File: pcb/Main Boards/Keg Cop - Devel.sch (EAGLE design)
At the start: 24 parts

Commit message: Add proper value for R6
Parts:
- R6: value 2.2kΩ -> 200kΩ
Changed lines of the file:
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@@
 <part name="SOLENOID" library="adafruit" library_urn="urn:adsk.eagle:library:420" deviceset="LED" device="3MM" package3d_urn="urn:adsk.eagle:package:6240537/1"/>
 <part name="COOL" library="adafruit" library_urn="urn:adsk.eagle:library:420" deviceset="LED" device="3MM" package3d_urn="urn:adsk.eagle:package:6240537/1"/>
-<part name="R6" library="SparkFun-Resistors" library_urn="urn:adsk.eagle:library:532" deviceset="RESISTOR" device="AXIAL-0.3" package3d_urn="urn:adsk.eagle:package:39658/1" value="2.2kΩ"/>
+<part name="R6" library="SparkFun-Resistors" library_urn="urn:adsk.eagle:library:532" deviceset="RESISTOR" device="AXIAL-0.3" package3d_urn="urn:adsk.eagle:package:39658/1" value="200kΩ"/>
 <part name="KEG" library="SparkFun-Sensors" deviceset="DS18B20" device=""/>
 <part name="LOWER" library="SparkFun-Sensors" deviceset="DS18B20" device=""/>

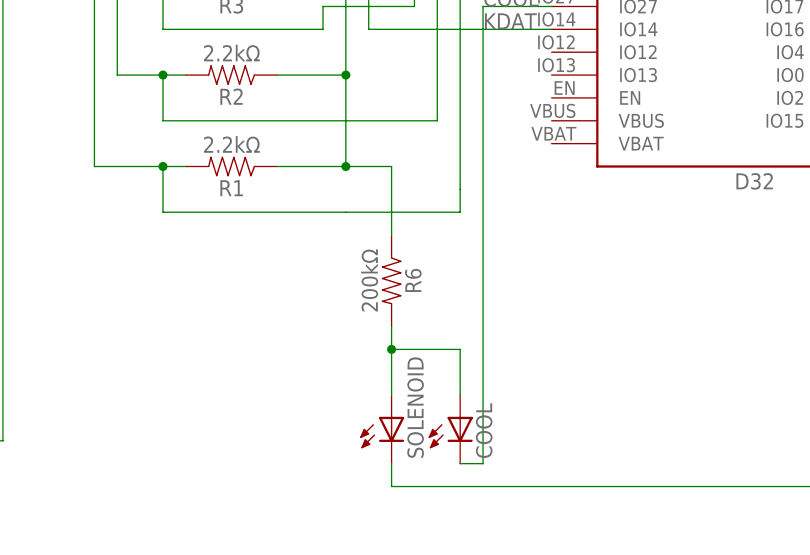
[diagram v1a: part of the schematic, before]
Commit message: Add separate power for sol/cool
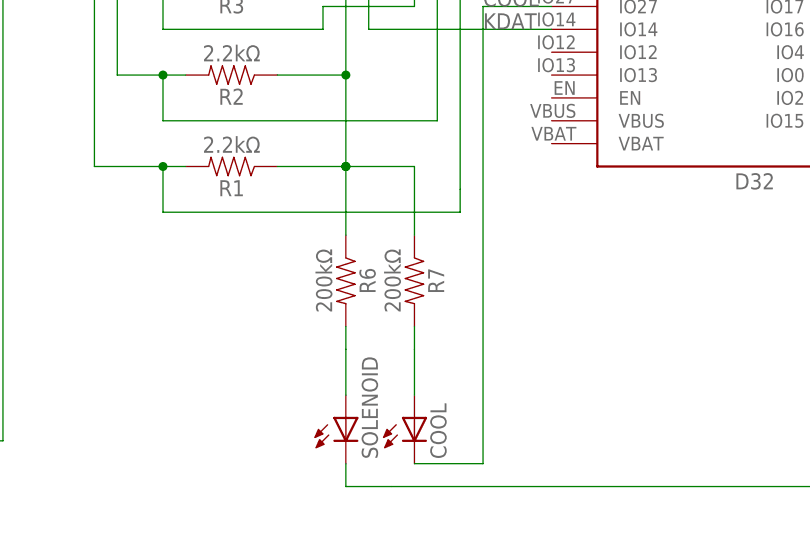
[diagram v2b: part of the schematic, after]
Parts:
- added R7: 200kΩ, SparkFun-Resistors:RESISTORAXIAL-0.3
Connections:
- new net N$1: COOL.A, R7.2
- net 3V3: now also R7.1
- net N$2: no longer COOL.A
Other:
- moved on the sheet: COOL, R6, SOLENOID
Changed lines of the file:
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@@
 <?xml version="1.0" encoding="utf-8"?>
 <!DOCTYPE eagle SYSTEM "eagle.dtd">
-<eagle version="9.5.2">
+<eagle version="9.6.2">
 <drawing>
 <settings>
@@
 <part name="TOWER" library="SparkFun-Sensors" deviceset="DS18B20" device=""/>
 <part name="ROOM" library="SparkFun-Sensors" deviceset="DS18B20" device=""/>
+<part name="R7" library="SparkFun-Resistors" library_urn="urn:adsk.eagle:library:532" deviceset="RESISTOR" device="AXIAL-0.3" package3d_urn="urn:adsk.eagle:package:39658/1" value="200kΩ"/>
 </parts>
 <sheets>
@@
 <attribute name="VALUE" x="76.835" y="100.33" size="1.778" layer="96"/>
 </instance>
-<instance part="SOLENOID" gate="G$1" x="-7.62" y="0" smashed="yes">
-<attribute name="NAME" x="-4.064" y="-4.572" size="1.778" layer="95" rot="R90"/>
-<attribute name="VALUE" x="-1.905" y="-4.572" size="1.778" layer="96" rot="R90"/>
-</instance>
-<instance part="COOL" gate="G$1" x="0" y="0" smashed="yes">
-<attribute name="NAME" x="3.556" y="-4.572" size="1.778" layer="95" rot="R90"/>
-<attribute name="VALUE" x="5.715" y="-4.572" size="1.778" layer="96" rot="R90"/>
-</instance>
-<instance part="R6" gate="G$1" x="-7.62" y="15.24" smashed="yes" rot="R270">
-<attribute name="NAME" x="-6.096" y="15.24" size="1.778" layer="95" font="vector" rot="R270" align="bottom-center"/>
-<attribute name="VALUE" x="-9.144" y="15.24" size="1.778" layer="96" font="vector" rot="R270" align="top-center"/>
+<instance part="SOLENOID" gate="G$1" x="-12.7" y="0" smashed="yes">
+<attribute name="NAME" x="-9.144" y="-4.572" size="1.778" layer="95" rot="R90"/>
+<attribute name="VALUE" x="-6.985" y="-4.572" size="1.778" layer="96" rot="R90"/>
+</instance>
+<instance part="COOL" gate="G$1" x="-5.08" y="0" smashed="yes">
+<attribute name="NAME" x="-1.524" y="-4.572" size="1.778" layer="95" rot="R90"/>
+<attribute name="VALUE" x="0.635" y="-4.572" size="1.778" layer="96" rot="R90"/>
+</instance>
+<instance part="R6" gate="G$1" x="-12.7" y="15.24" smashed="yes" rot="R270">
+<attribute name="NAME" x="-11.176" y="15.24" size="1.778" layer="95" font="vector" rot="R270" align="bottom-center"/>
+<attribute name="VALUE" x="-14.224" y="15.24" size="1.778" layer="96" font="vector" rot="R270" align="top-center"/>
 </instance>
 <instance part="KEG" gate="G$1" x="-73.66" y="78.74" smashed="yes" rot="R180">
@@
 <attribute name="NAME" x="-66.04" y="-10.414" size="1.778" layer="95" font="vector" rot="R180"/>
 <attribute name="VALUE" x="-66.04" y="5.334" size="1.778" layer="96" font="vector" rot="R180" align="top-left"/>
+</instance>
+<instance part="R7" gate="G$1" x="-5.08" y="15.24" smashed="yes" rot="R270">
+<attribute name="NAME" x="-3.556" y="15.24" size="1.778" layer="95" font="vector" rot="R270" align="bottom-center"/>
+<attribute name="VALUE" x="-6.604" y="15.24" size="1.778" layer="96" font="vector" rot="R270" align="top-center"/>
 </instance>
 </instances>
@@
 <label x="-48.26" y="63.5" size="1.778" layer="95"/>
 <pinref part="R6" gate="G$1" pin="1"/>
-<wire x1="-7.62" y1="20.32" x2="-7.62" y2="27.94" width="0.1524" layer="91"/>
-<wire x1="-7.62" y1="27.94" x2="-12.7" y2="27.94" width="0.1524" layer="91"/>
+<wire x1="-12.7" y1="20.32" x2="-12.7" y2="27.94" width="0.1524" layer="91"/>
 <junction x="-12.7" y="27.94"/>
 <pinref part="KEG" gate="G$1" pin="VDD"/>
@@
 <wire x1="-48.26" y1="63.5" x2="-58.42" y2="63.5" width="0.1524" layer="91"/>
 <junction x="-58.42" y="63.5"/>
+<pinref part="R7" gate="G$1" pin="1"/>
+<wire x1="-5.08" y1="20.32" x2="-5.08" y2="27.94" width="0.1524" layer="91"/>
+<wire x1="-5.08" y1="27.94" x2="-12.7" y2="27.94" width="0.1524" layer="91"/>
+<junction x="-12.7" y="27.94"/>
 </segment>
 </net>
@@
 <label x="2.54" y="45.72" size="1.778" layer="95"/>
 <wire x1="2.54" y1="45.72" x2="2.54" y2="-5.08" width="0.1524" layer="91"/>
-<wire x1="0" y1="-5.08" x2="2.54" y2="-5.08" width="0.1524" layer="91"/>
+<wire x1="-5.08" y1="-5.08" x2="2.54" y2="-5.08" width="0.1524" layer="91"/>
 <pinref part="COOL" gate="G$1" pin="C"/>
 </segment>
@@
 <wire x1="-7.62" y1="-7.62" x2="55.88" y2="-7.62" width="0.1524" layer="91"/>
 <pinref part="SOLENOID" gate="G$1" pin="C"/>
-<wire x1="-7.62" y1="-5.08" x2="-7.62" y2="-7.62" width="0.1524" layer="91"/>
+<wire x1="-12.7" y1="-5.08" x2="-12.7" y2="-7.62" width="0.1524" layer="91"/>
+<wire x1="-12.7" y1="-7.62" x2="-7.62" y2="-7.62" width="0.1524" layer="91"/>
 </segment>
 </net>
 <net name="N$2" class="0">
 <segment>
-<wire x1="0" y1="7.62" x2="-7.62" y2="7.62" width="0.1524" layer="91"/>
 <pinref part="R6" gate="G$1" pin="2"/>
-<wire x1="-7.62" y1="7.62" x2="-7.62" y2="10.16" width="0.1524" layer="91"/>
+<wire x1="-12.7" y1="7.62" x2="-12.7" y2="10.16" width="0.1524" layer="91"/>
 <pinref part="SOLENOID" gate="G$1" pin="A"/>
-<wire x1="-7.62" y1="2.54" x2="-7.62" y2="7.62" width="0.1524" layer="91"/>
-<junction x="-7.62" y="7.62"/>
+<wire x1="-12.7" y1="2.54" x2="-12.7" y2="7.62" width="0.1524" layer="91"/>
+</segment>
+</net>
+<net name="N$1" class="0">
+<segment>
 <pinref part="COOL" gate="G$1" pin="A"/>
-<wire x1="0" y1="7.62" x2="0" y2="2.54" width="0.1524" layer="91"/>
-</segment>
-</net>
+<wire x1="-5.08" y1="7.62" x2="-5.08" y2="2.54" width="0.1524" layer="91"/>
+<pinref part="R7" gate="G$1" pin="2"/>
+<wire x1="-5.08" y1="7.62" x2="-5.08" y2="10.16" width="0.1524" layer="91"/>
+</segment>
+</net>
